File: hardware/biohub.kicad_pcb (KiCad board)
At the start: 4 copper layers, 89 x 55 mm, 131 parts, among them J1 CONNECTOR, J2 Conn_02x13_Odd_Even, U1 ADUM1412BRWZ, U10 AD8244BRMZ, U11 AD8244BRMZ, U12 TPD4E1B06DCKR, U13 TPD4E1B06DCKR, U14 MCP1603T-330I, U2 MCP2210-I_SS, U3 ADUM6020, U4 ADM8660ARZ, U5 ADP7142AUJZ-2.5-R7, U6 ADP7182AUJZ-2.5-R7, U7 ADS1299IPAG, U8 AD8244BRMZ, U9 AD8244BRMZ

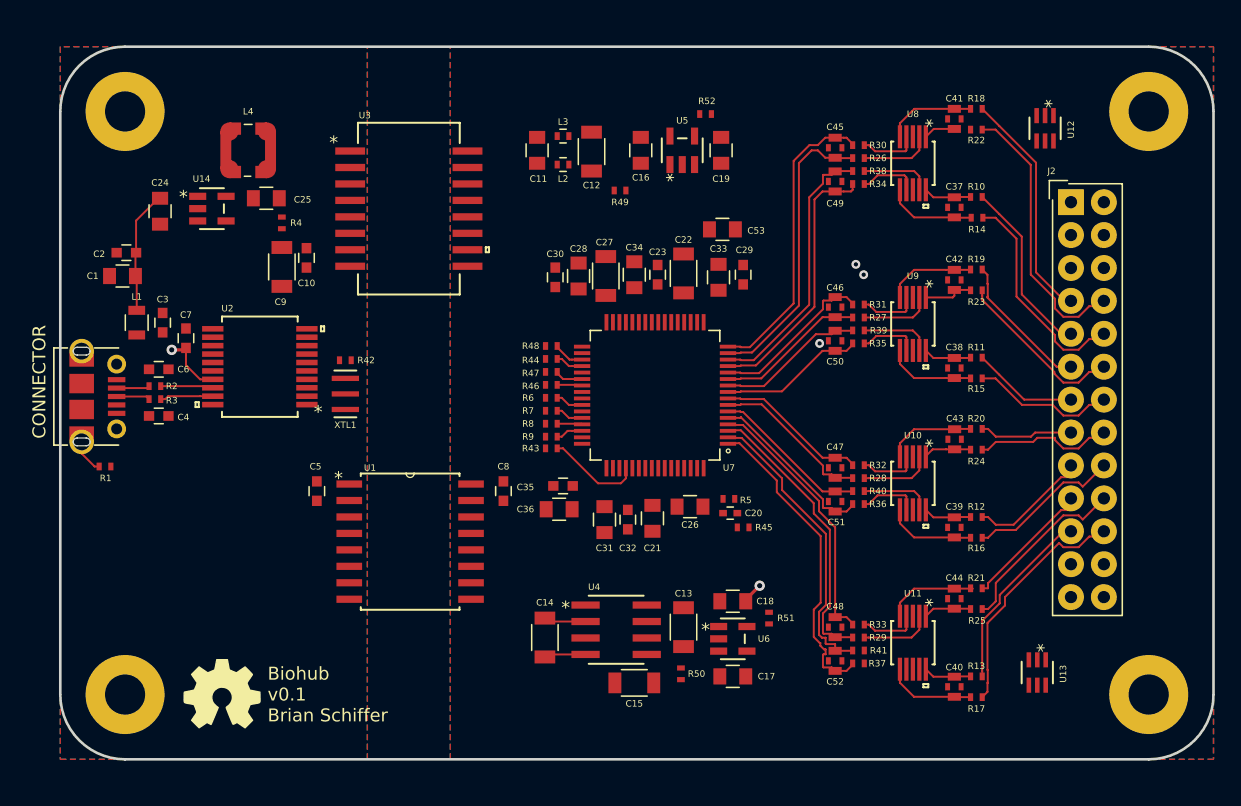
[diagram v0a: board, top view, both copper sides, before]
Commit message: Started layout
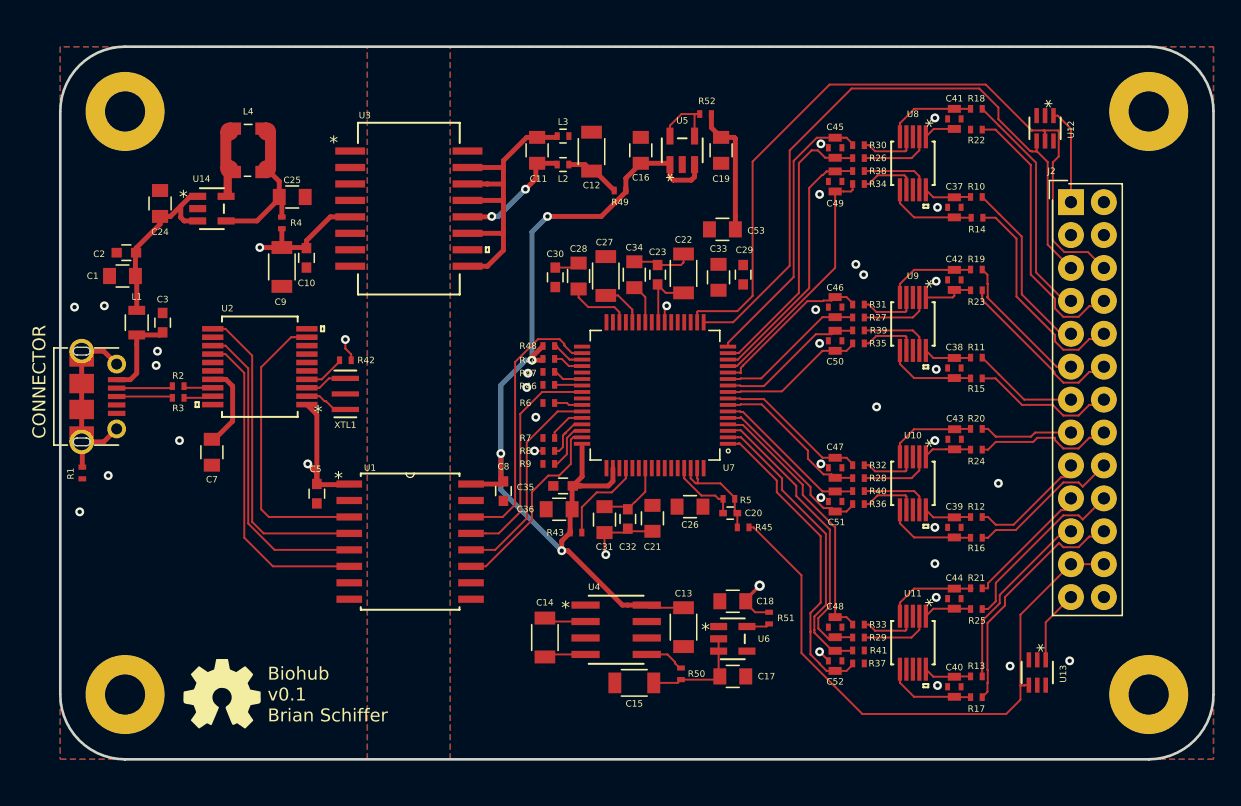
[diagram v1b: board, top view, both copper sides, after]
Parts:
- removed C4, C6: 47p, Capacitors_SMD:C_0603
- C7: value 0.1u -> 0.22u; footprint Capacitors_SMD:C_0603 -> Capacitors_SMD:C_0805
- moved C7 9.02 mm to (116.2, 96.3), turned to 270 degrees
- moved R43 6.77 mm to (144.3, 102.5)
- moved R7 2.11 mm to (142.2, 95.2)
- moved R8 2.11 mm to (142.2, 96.2)
- moved R9 2.11 mm to (142.2, 97.2)
- moved C25 2.00 mm to (122.4, 76.6), turned to 0 degrees
- moved R1 1.82 mm to (106.2, 97.9), turned to 270 degrees
- moved R3 1.80 mm to (113.6, 92.1)
- moved R2 1.80 mm to (113.6, 91.2)
- moved C24 0.60 mm to (112.2, 77.1), turned to 90 degrees
- moved R6 0.45 mm to (142.2, 92.5)
- moved R44 0.20 mm to (142.2, 89.1)
- moved R46 0.20 mm to (142.2, 91.1)
- moved R47 0.20 mm to (142.2, 90.1)
- moved R48 0.20 mm to (142.2, 88.1)
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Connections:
- net Net-(C11-Pad1) renamed /usb/ISO_VDD_1
- net Net-(C11-Pad2) renamed /usb/ISO
- net Net-(C12-Pad1) renamed /usb/ISO_VDD_2
- net Net-(C25-Pad1) renamed /usb/Vfb
- net Net-(C3-Pad1) renamed /usb/VUSB
- net Net-(J1-PadSH1) renamed /usb/SHLD
- net Net-(L4-Pad1) renamed /usb/LX
- C48 pad 3: Net-(C48-Pad3) -> GND
- J2 pad 23: /AFE/SRB2 -> /AFE/BIAS
- J2 pad 24: /AFE/SRB1 -> /AFE/BIAS
- J2 pad 5: /AFE/BIAS -> /AFE/SRB1
- J2 pad 6: /AFE/BIAS -> /AFE/SRB2
- U1 pad 13: /AFE/MOSI -> /AFE/SCLK
- U1 pad 14: GND -> /AFE/MOSI
- U1 pad 3: GNDD -> /usb/USB_SPI_MOSI
- U1 pad 4: /usb/USB_SPI_MOSI -> /usb/USB_SPI_CLK
- U10 pad 8: +2V5 -> -2V5
- U11 pad 8: +2V5 -> -2V5
- U12 pad 4: /AFE/BIAS -> /AFE/SRB1
- U12 pad 5: Net-(U12-Pad5) -> /AFE/SRB2
- U13 pad 1: /AFE/SRB2 -> -2V5
- U13 pad 4: -2V5 -> /AFE/BIAS
- U13 pad 5: /AFE/SRB1 -> Net-(U13-Pad5)
- U2 pad 1: VBUS -> VCOM
- U2 pad 11: GNDD -> /usb/USB_SPI_CLK
- U7 pad 40: GND -> /AFE/SCLK
- U8 pad 8: +2V5 -> -2V5
- U9 pad 8: +2V5 -> -2V5
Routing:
- net +3V3: track 0.00 -> 77.3 mm, vias 0 -> 4
- net /AFE/SRB2: track 0.00 -> 57.9 mm
- net /AFE/SRB1: track 0.00 -> 51.9 mm
- net /AFE/BIAS: track 0.00 -> 46.2 mm
- net /usb/ISO: track 0.00 -> 26.3 mm
- net /usb/USB_SPI_DATA_READY: track 0.00 -> 24.8 mm
- net /usb/USB_SPI_CLK: track 0.00 -> 24.6 mm
- net /usb/USB_SPI_MISO: track 0.00 -> 24.1 mm
- net VCOM: track 5.02 -> 28.7 mm, vias 1 -> 3
- net /usb/USB_SPI_MOSI: track 0.00 -> 22.5 mm
- net -2V5: track 1.65 -> 23.1 mm, vias 1 -> 3
- net /AFE/MOSI: track 0.00 -> 21.2 mm
- net +2V5: track 0.00 -> 20.2 mm
- net /AFE/SCLK: track 0.00 -> 17.5 mm
- net /AFE/MISO: track 0.00 -> 16.4 mm
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- added copper zone on B.Cu, net GND
- added copper zone on In2.Cu, net GND
- added copper zone on In1.Cu, net GNDD
- added copper zone on In2.Cu, net GNDD
- removed copper zone on In2.Cu, net +2V5
- removed copper zone on In1.Cu, net +3V3
- removed copper zone on B.Cu, net -2V5
- removed copper zone on In1.Cu, net VCOM
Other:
- net class POWER added: clearance 0.1524, trace_width 0.381, via_dia 0.6858, via_drill 0.3302
- net class SIGNAL added: clearance 0.1524, trace_width 0.1524, via_dia 0.6858, via_drill 0.3302

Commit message: First full layout
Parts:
- moved C30 26.3 mm to (156.4, 105.3), turned to 180 degrees
- moved C22 5.19 mm to (150.9, 77.6), turned to 0 degrees
- moved C53 3.75 mm to (152.8, 81.6)
- moved R52 3.69 mm to (157.1, 72.6), turned to 270 degrees
- moved C10 3.14 mm to (120.6, 82.5), turned to 180 degrees
- moved C23 3.01 mm to (150.8, 79.6), turned to 0 degrees
- moved C9 2.41 mm to (119.8, 80.4), turned to 180 degrees
- moved R51 1.30 mm to (159.3, 107.8), turned to 0 degrees
- moved R50 0.42 mm to (152.7, 113.7), turned to 0 degrees
- moved C29 0.22 mm to (157.0, 82.7), turned to 90 degrees
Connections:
- net Net-(C14-Pad1) renamed /power/CP1
- net Net-(C14-Pad2) renamed /power/CP2
- C15 pad 1: -3V3 -> /power/INV_OUT
- C18 pad 1: -2V5 -> /power/n2_5_OUT
- C19 pad 1: +2V5 -> /power/2_5_OUT
- R50 pad 1: Net-(R50-Pad1) -> /power/INV_OUT
- R51 pad 1: Net-(R51-Pad1) -> /power/n2_5_OUT
- R52 pad 1: Net-(R52-Pad1) -> /power/2_5_OUT
- U4 pad 5: Net-(R50-Pad1) -> /power/INV_OUT
- U5 pad 4: Net-(R52-Pad1) -> /power/2_5_OUT
- U5 pad 5: Net-(R52-Pad1) -> /power/2_5_OUT
- U6 pad 5: Net-(R51-Pad1) -> /power/n2_5_OUT
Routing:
- net -2V5: track 23.1 -> 194.9 mm, vias 3 -> 14
- net +2V5: track 20.2 -> 177.0 mm, vias 0 -> 7
- net VCOM: track 28.7 -> 59.6 mm
- net GND: track 1.63 -> 27.8 mm, vias 24 -> 275
- net /power/2_5_OUT: track 0.00 -> 8.01 mm
- net Net-(R41-Pad2): track 0.00 -> 6.24 mm
- net Net-(R52-Pad1): track 5.20 -> 0.00 mm
- net Net-(R37-Pad2): track 0.00 -> 4.79 mm
- net /power/INV_OUT: track 0.00 -> 4.62 mm
- net Net-(C22-Pad2): track 5.22 -> 9.48 mm
- net /power/n2_5_OUT: track 0.00 -> 3.44 mm
- net Net-(R50-Pad1): track 3.13 -> 0.00 mm
- net +3V3: track 77.3 -> 79.2 mm, vias 4 -> 5
- net Net-(R51-Pad1): track 1.79 -> 0.00 mm
- net Net-(C41-Pad2): track 2.45 -> 3.72 mm
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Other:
- net class POWER: trace_width 0.381 -> 0.3048

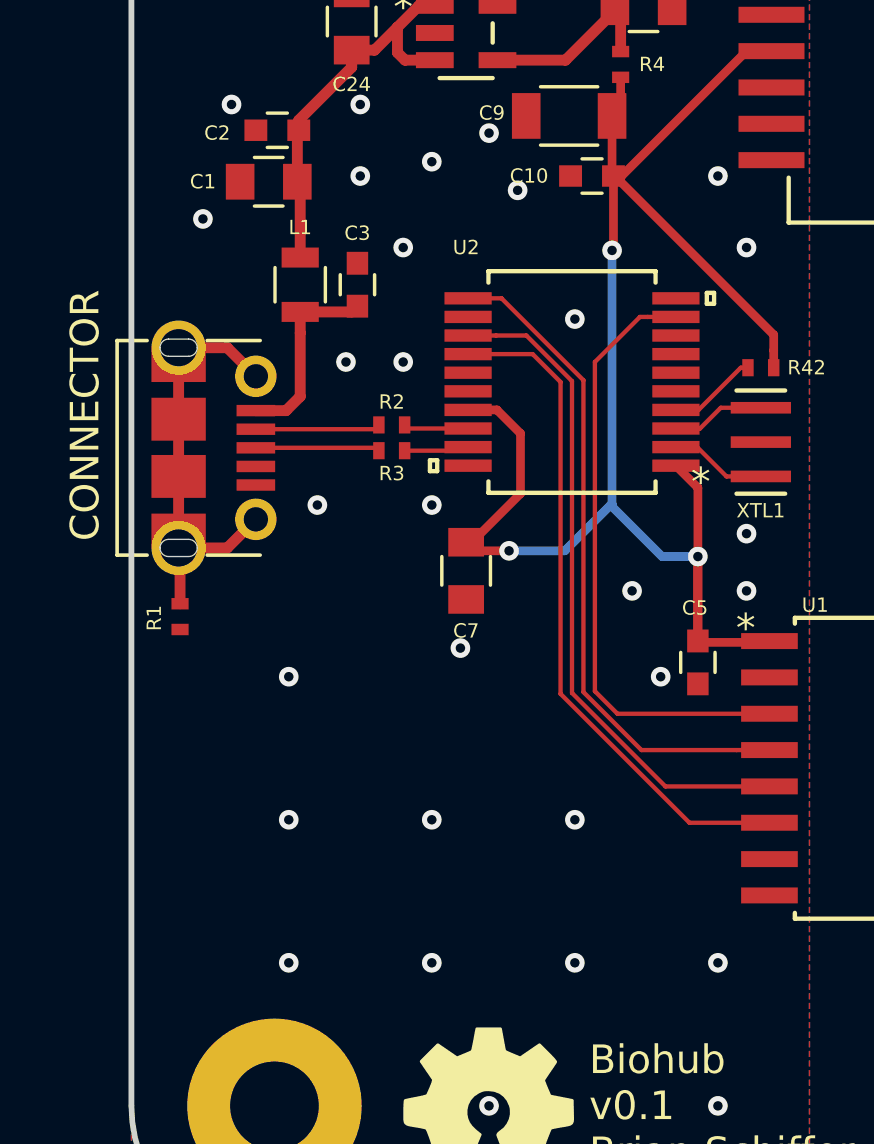
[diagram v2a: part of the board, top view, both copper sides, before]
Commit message: Added USB ESD Protection
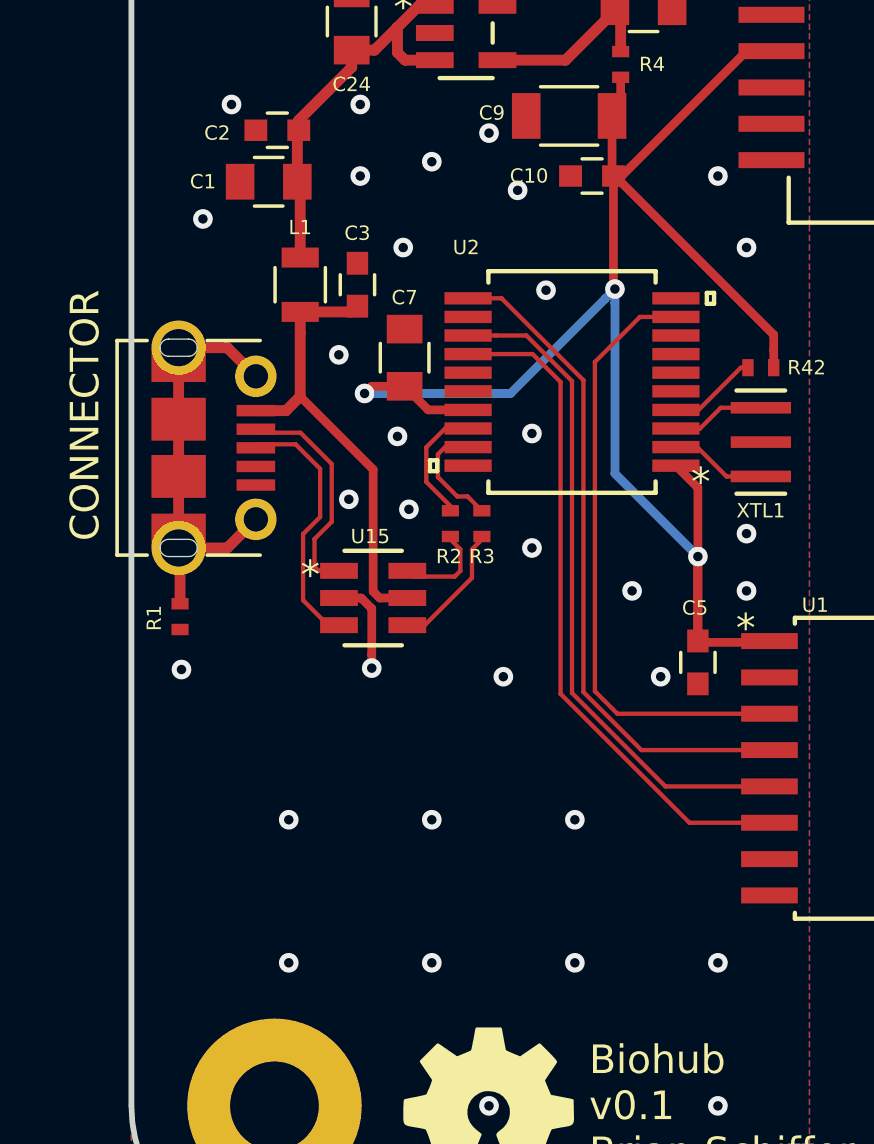
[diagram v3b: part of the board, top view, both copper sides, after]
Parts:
- added U15: USBLC6-2SC6, biohub:USBLC62, F.Cu at (113.0, 97.2)
- moved C7 7.75 mm to (114.0, 88.8), turned to 90 degrees
- moved R3 4.05 mm to (116.8, 94.7), turned to 270 degrees
- moved R2 4.01 mm to (115.7, 94.7), turned to 270 degrees
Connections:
- net Net-(R2-Pad1) renamed /usb/MCP_D-
- net Net-(R3-Pad1) renamed /usb/MCP_D+
- J1 pad 2: Net-(J1-Pad2) -> /usb/USB_D-
- J1 pad 3: Net-(J1-Pad3) -> /usb/USB_D+
- R2 pad 2: Net-(J1-Pad2) -> /usb/ESD_D-
- R3 pad 2: Net-(J1-Pad3) -> /usb/ESD_D+
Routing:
- net /usb/VUSB: track 6.79 -> 16.0 mm
- net /usb/USB_D+: track 0.00 -> 9.11 mm
- net /usb/USB_D-: track 0.00 -> 7.91 mm
- net /usb/ESD_D+: track 0.00 -> 4.53 mm
- net Net-(J1-Pad2): track 4.36 -> 0.00 mm
- net Net-(J1-Pad3): track 4.34 -> 0.00 mm
- net GNDD: track 0.00 -> 3.38 mm, vias 38 -> 41
- net /usb/ESD_D-: track 0.00 -> 3.36 mm
- net /usb/MCP_D-: track 2.27 -> 4.30 mm
- net /usb/MCP_D+: track 2.27 -> 3.98 mm
- net VCOM: track 59.6 -> 60.4 mm
